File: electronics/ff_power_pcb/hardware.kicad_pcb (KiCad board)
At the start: 4 copper layers, 60 x 37 mm, 60 parts, among them J1 Conn_01x01_Female, J2 Conn_01x01_Female, J3 Conn_01x07_Male, U3 TPS62095RGTR, U4 TPS62095RGTR, U5 TPS62095RGTR, U6 TPS62095RGTR, U7 AP131-25

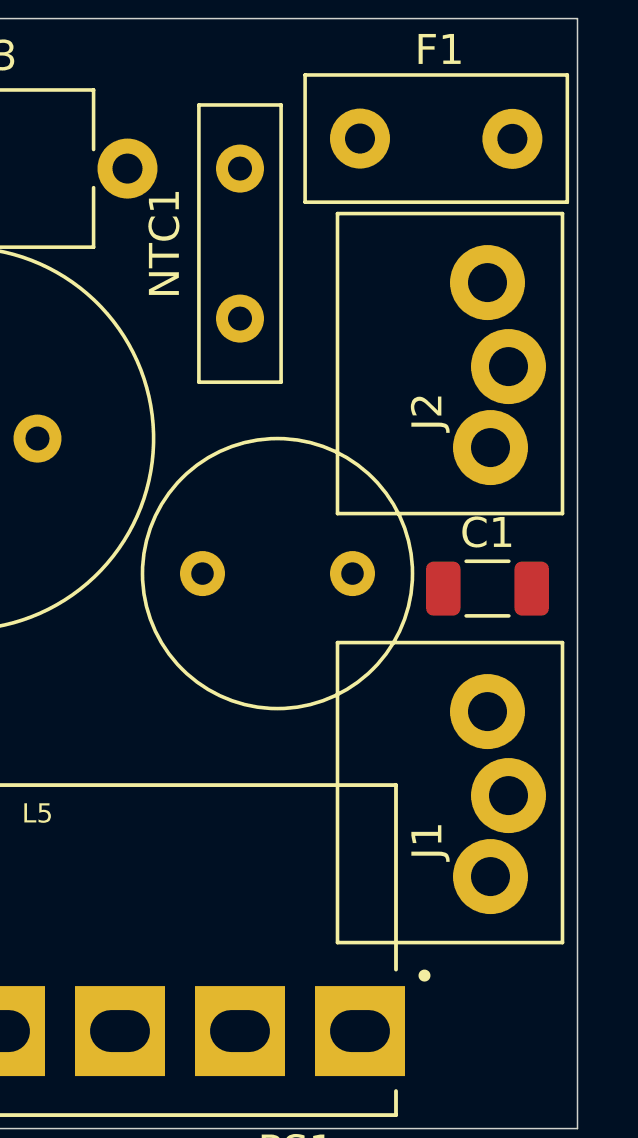
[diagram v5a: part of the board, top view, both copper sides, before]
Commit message: Alligned the blade connectors
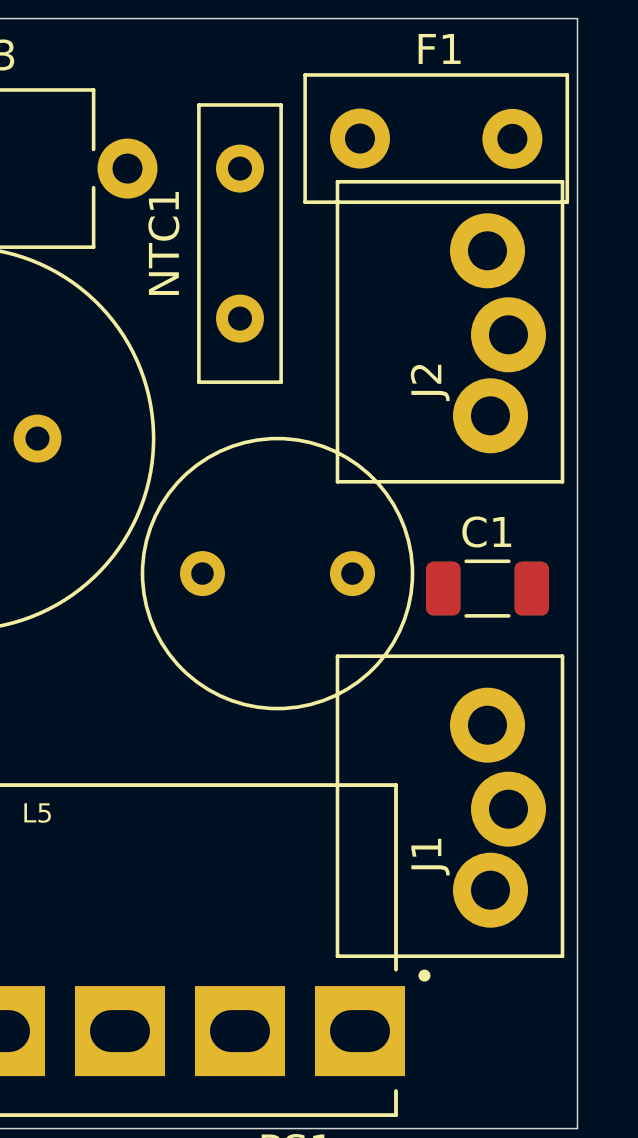
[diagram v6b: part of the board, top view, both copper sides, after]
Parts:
- moved J2 1.06 mm to (143.0, 106.4)
- moved J1 0.45 mm to (143.0, 122.3)
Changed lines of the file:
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@@
   )
   (module mains_blade:IRL_00 (layer F.Cu)
-    (at 143 107.5 90)
+    (at 143 106.440814 90)
     (fp_text reference J2 (at 1.4 -2 90) (layer F.SilkS)
       (effects (font (size 1 1) (thickness 0.15)))
@@
   )
   (module mains_blade:IRL_00 (layer F.Cu)
-    (at 143 121.8 90)
+    (at 143 122.254 90)
     (fp_text reference J1 (at 1.4 -2 90) (layer F.SilkS)
       (effects (font (size 1 1) (thickness 0.15)))

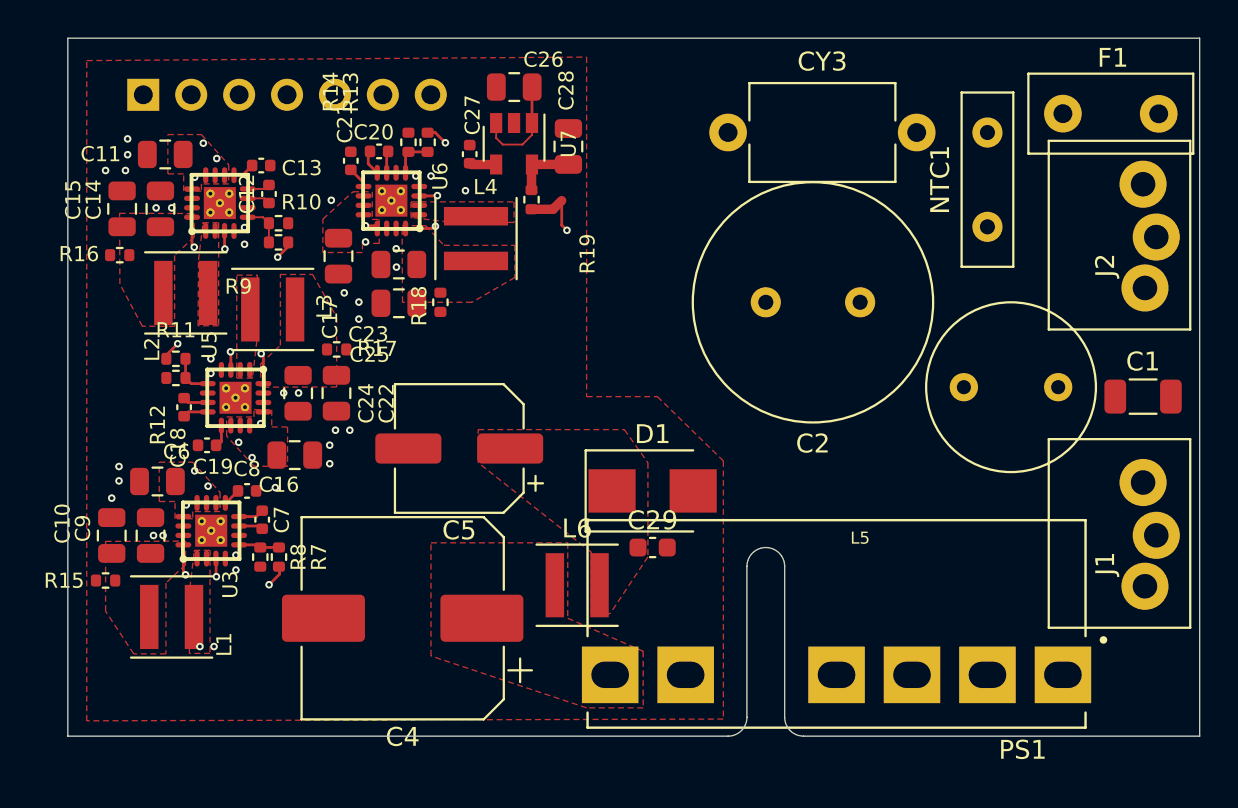
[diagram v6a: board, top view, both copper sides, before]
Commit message: Finished up the routing on the power board, still needs a double check.
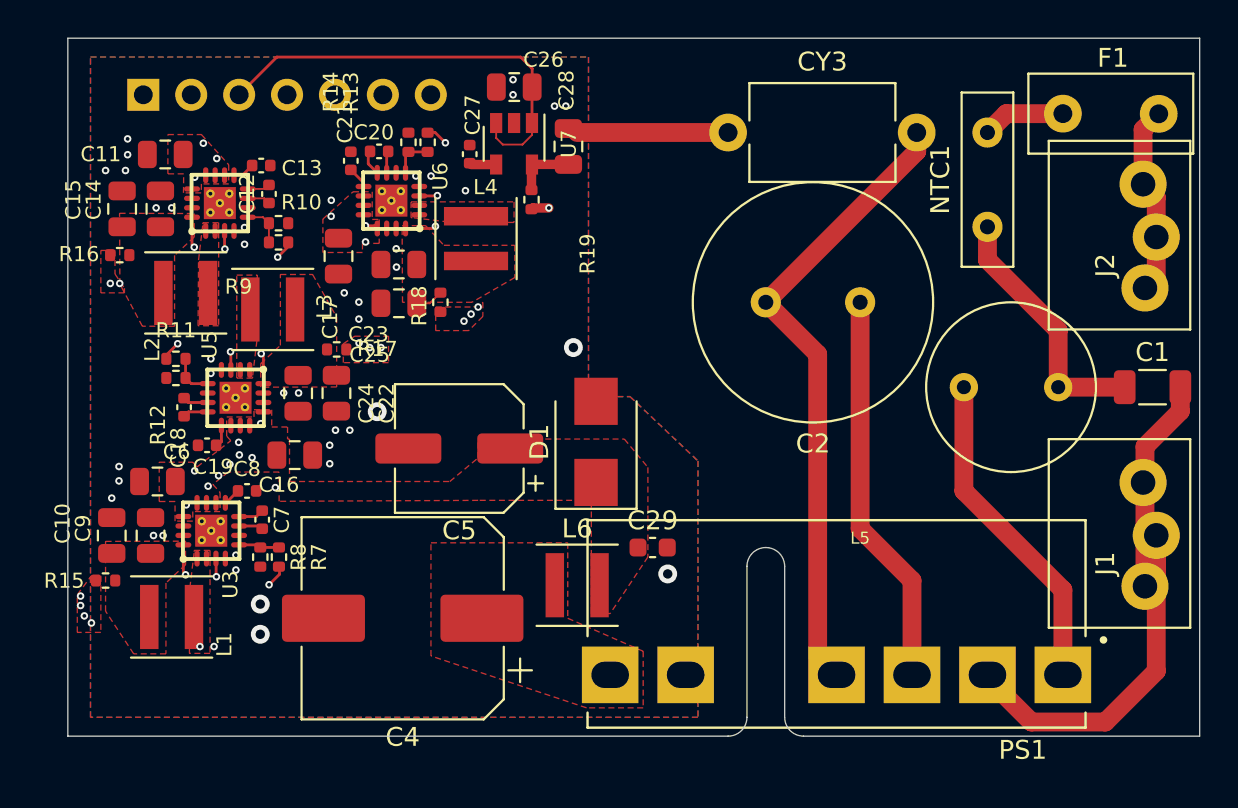
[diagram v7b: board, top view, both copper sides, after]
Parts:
- moved D1 3.97 mm to (114.0, 114.4), turned to 90 degrees
- moved C1 0.71 mm to (143.5, 111.5)
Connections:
- J3 pad 1: Net-(J3-Pad1) -> GND
- J3 pad 2: Net-(J3-Pad2) -> +5V
- J3 pad 3: Net-(J3-Pad3) -> +3V3
- J3 pad 4: Net-(J3-Pad4) -> +3V0
- J3 pad 5: Net-(J3-Pad5) -> +2V5
- J3 pad 6: Net-(J3-Pad6) -> +1V35
- J3 pad 7: Net-(J3-Pad7) -> +1V1
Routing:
- net +3V3: track 6.42 -> 62.6 mm, vias 0 -> 4
- net Net-(C2-Pad2): track 0.00 -> 33.6 mm
- net /AC_N: track 0.00 -> 32.7 mm
- net +5V: track 23.2 -> 53.3 mm, vias 15 -> 19
- net Net-(C2-Pad1): track 0.00 -> 20.9 mm
- net +3V0: track 0.00 -> 20.0 mm, vias 0 -> 2
- net Net-(L5-Pad2): track 0.00 -> 17.4 mm
- net +1V35: track 0.00 -> 16.5 mm, vias 0 -> 3
- net Net-(C1-Pad1): track 0.00 -> 13.6 mm
- net +1V1: track 0.00 -> 13.5 mm, vias 0 -> 3
- net +2V5: track 3.48 -> 16.7 mm
- net /AC_L: track 0.00 -> 9.42 mm
- net GND: track 0.00 -> 8.50 mm, vias 34 -> 43
- net Net-(F1-Pad1): track 0.00 -> 4.41 mm
- net Net-(C23-Pad1): track 7.29 -> 8.78 mm
- added copper zone on F.Cu, net +1V1
- added copper zone on F.Cu, net +1V35
- added copper zone on F.Cu, net +3V0
- added copper zone on F.Cu, net +3V3
- added copper zone on B.Cu, net GND
- added copper zone on In2.Cu, net GND

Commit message: Worked on the routing.
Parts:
- moved D1 2.19 mm to (112.0, 113.5)
- moved CY3 2.02 mm to (121.2, 96.0)
- moved C5 1.75 mm to (105.0, 114.8)
- moved C21 0.72 mm to (100.5, 100.0), turned to 180 degrees
- moved C13 0.71 mm to (95.8, 99.2), turned to 90 degrees
- moved C7 0.28 mm to (96.3, 118.2)
- moved C12 0.26 mm to (96.7, 101.0)
- moved C20 0.25 mm to (102.2, 99.0)
- moved C8 0.25 mm to (95.2, 117.0), turned to 90 degrees
- moved L6 0.25 mm to (113.0, 121.8)
- moved C18 0.19 mm to (92.2, 112.8)
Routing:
- net Net-(C2-Pad2): track 33.6 -> 35.7 mm
- net GND: track 8.50 -> 9.50 mm, vias 43 -> 42
- added copper zone on In1.Cu, net GND
